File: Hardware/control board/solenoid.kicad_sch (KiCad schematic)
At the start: 7 parts, among them J11 Screw_Terminal_01x02, Q3 NMOS

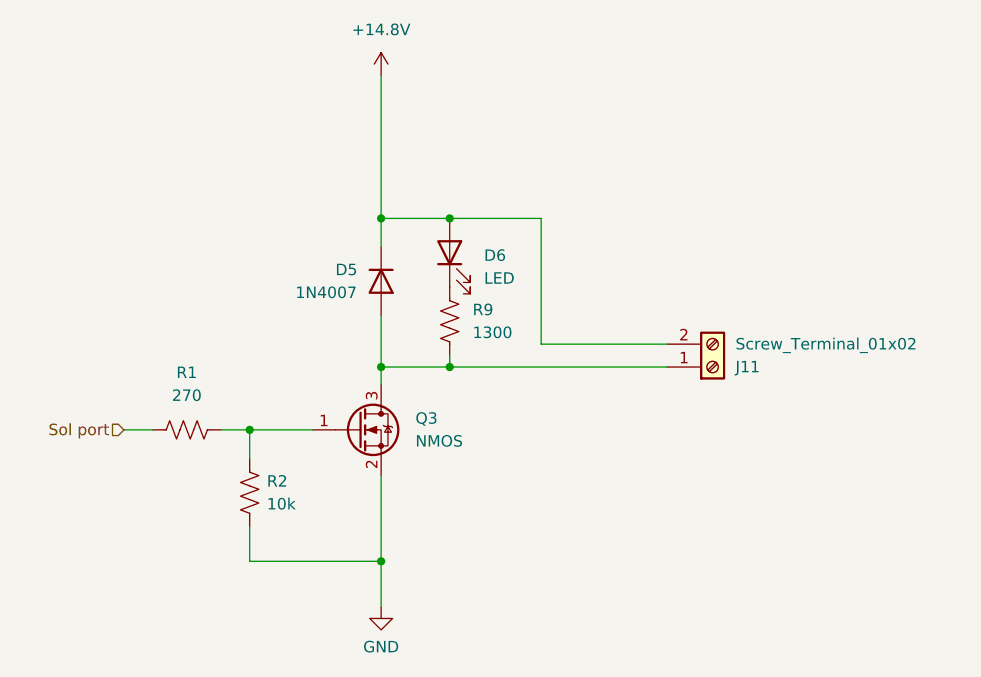
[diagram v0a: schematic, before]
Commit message: fixed github problems
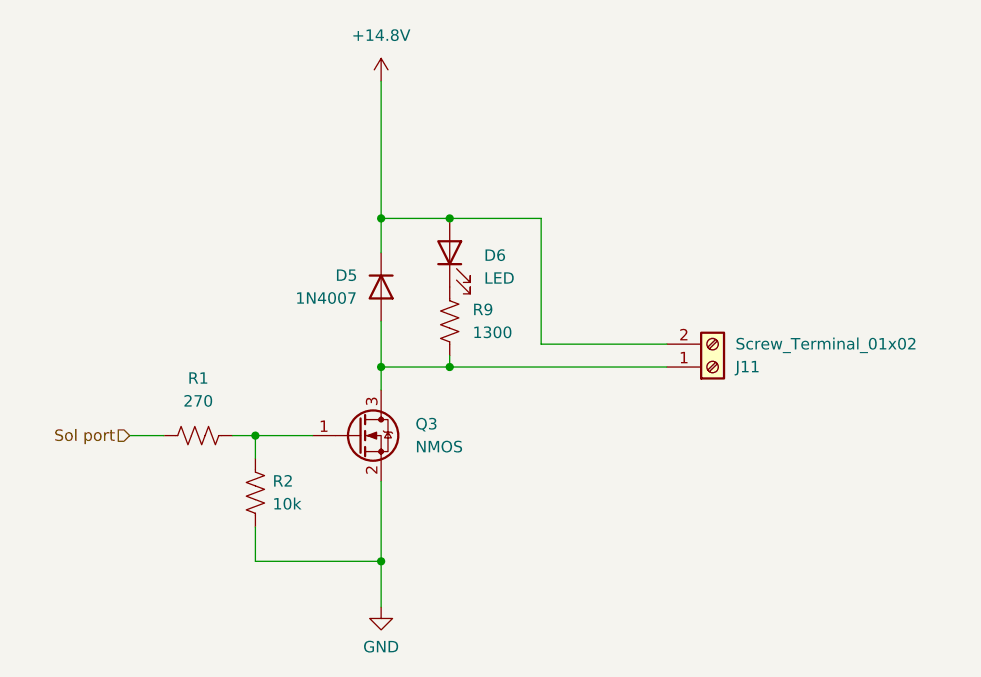
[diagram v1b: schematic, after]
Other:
- moved on the sheet: D5, Q3, R1, R2
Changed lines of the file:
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@@
   (junction (at 121.92 76.2) (diameter 0) (color 0 0 0 0)
   )
-  (junction (at 107.315 99.695) (diameter 0) (color 0 0 0 0)
-  )
   (junction (at 129.54 76.2) (diameter 0) (color 0 0 0 0)
   )
@@
   (junction (at 121.92 114.3) (diameter 0) (color 0 0 0 0)
   )
-  (wire (pts (xy 107.315 110.49) (xy 107.315 114.3))
-    (stroke (width 0) (type default))
-  )
-  (wire (pts (xy 107.315 99.695) (xy 114.3 99.695))
-    (stroke (width 0) (type default))
-  )
-  (wire (pts (xy 107.315 99.695) (xy 107.315 102.87))
-    (stroke (width 0) (type default))
-  )
-  (wire (pts (xy 107.315 114.3) (xy 121.92 114.3))
+  (junction (at 107.95 100.33) (diameter 0) (color 0 0 0 0)
+  )
+  (wire (pts (xy 107.95 110.49) (xy 107.95 114.3))
+    (stroke (width 0) (type default))
+  )
+  (wire (pts (xy 93.98 100.33) (xy 97.79 100.33))
+    (stroke (width 0) (type default))
+  )
+  (wire (pts (xy 107.95 114.3) (xy 121.92 114.3))
     (stroke (width 0) (type default))
   )
@@
     (stroke (width 0) (type default))
   )
-  (wire (pts (xy 93.345 99.695) (xy 96.52 99.695))
-    (stroke (width 0) (type default))
-  )
-  (wire (pts (xy 121.92 86.995) (xy 121.92 92.71))
-    (stroke (width 0) (type default))
-  )
-  (wire (pts (xy 121.92 92.71) (xy 121.92 94.615))
+  (wire (pts (xy 121.92 87.63) (xy 121.92 92.71))
+    (stroke (width 0) (type default))
+  )
+  (wire (pts (xy 121.92 92.71) (xy 121.92 95.25))
     (stroke (width 0) (type default))
   )
@@
     (stroke (width 0) (type default))
   )
+  (wire (pts (xy 121.92 60.96) (xy 121.92 76.2))
+    (stroke (width 0) (type default))
+  )
+  (wire (pts (xy 107.95 100.33) (xy 107.95 102.87))
+    (stroke (width 0) (type default))
+  )
   (wire (pts (xy 129.54 76.2) (xy 139.7 76.2))
     (stroke (width 0) (type default))
@@
     (stroke (width 0) (type default))
   )
-  (wire (pts (xy 107.315 99.695) (xy 104.14 99.695))
-    (stroke (width 0) (type default))
-  )
-  (wire (pts (xy 121.92 104.775) (xy 121.92 114.3))
+  (wire (pts (xy 105.41 100.33) (xy 107.95 100.33))
+    (stroke (width 0) (type default))
+  )
+  (wire (pts (xy 107.95 100.33) (xy 114.3 100.33))
+    (stroke (width 0) (type default))
+  )
+  (wire (pts (xy 121.92 105.41) (xy 121.92 114.3))
     (stroke (width 0) (type default))
   )
@@
     (stroke (width 0) (type default))
   )
-  (wire (pts (xy 121.92 76.2) (xy 121.92 79.375))
-    (stroke (width 0) (type default))
-  )
-  (wire (pts (xy 121.92 60.325) (xy 121.92 76.2))
-    (stroke (width 0) (type default))
-  )
-  (hierarchical_label "Sol port" (shape input) (at 93.345 99.695 180) (fields_autoplaced)
+  (wire (pts (xy 121.92 76.2) (xy 121.92 80.01))
+    (stroke (width 0) (type default))
+  )
+  (hierarchical_label "Sol port" (shape input) (at 93.98 100.33 180) (fields_autoplaced)
     (effects (font (size 1.27 1.27)) (justify right))
   )
-  (symbol (lib_id "Transistor_FET:2N7002") (at 119.38 99.695 0) (unit 1)
-    (in_bom yes) (on_board yes) (dnp no) (fields_autoplaced)
-    (property "Reference" "Q3" (at 125.73 98.425 0)
-      (effects (font (size 1.27 1.27)) (justify left))
-    )
-    (property "Value" "NMOS" (at 125.73 100.965 0)
-      (effects (font (size 1.27 1.27)) (justify left))
-    )
-    (property "Footprint" "Package_TO_SOT_SMD:SOT-23" (at 124.46 101.6 0)
+  (symbol (lib_id "Transistor_FET:2N7002") (at 119.38 100.33 0) (unit 1)
+    (in_bom yes) (on_board yes) (dnp no) (fields_autoplaced)
+    (property "Reference" "Q3" (at 125.73 99.06 0)
+      (effects (font (size 1.27 1.27)) (justify left))
+    )
+    (property "Value" "NMOS" (at 125.73 101.6 0)
+      (effects (font (size 1.27 1.27)) (justify left))
+    )
+    (property "Footprint" "Package_TO_SOT_SMD:SOT-23" (at 124.46 102.235 0)
       (effects (font (size 1.27 1.27) italic) (justify left) hide)
     )
-    (property "Datasheet" "https://www.onsemi.com/pub/Collateral/NDS7002A-D.PDF" (at 119.38 99.695 0)
+    (property "Datasheet" "https://www.onsemi.com/pub/Collateral/NDS7002A-D.PDF" (at 119.38 100.33 0)
       (effects (font (size 1.27 1.27)) (justify left) hide)
     )
-    (property "Sim.Device" "NMOS" (at 119.38 116.84 0)
-      (effects (font (size 1.27 1.27)) hide)
-    )
-    (property "Sim.Type" "VDMOS" (at 119.38 118.745 0)
-      (effects (font (size 1.27 1.27)) hide)
-    )
-    (property "Sim.Pins" "1=D 2=G 3=S" (at 119.38 114.935 0)
+    (property "Sim.Device" "NMOS" (at 119.38 117.475 0)
+      (effects (font (size 1.27 1.27)) hide)
+    )
+    (property "Sim.Type" "VDMOS" (at 119.38 119.38 0)
+      (effects (font (size 1.27 1.27)) hide)
+    )
+    (property "Sim.Pins" "1=D 2=G 3=S" (at 119.38 115.57 0)
       (effects (font (size 1.27 1.27)) hide)
     )
@@
     )
   )
-  (symbol (lib_id "Device:R_US") (at 100.33 99.695 90) (unit 1)
-    (in_bom yes) (on_board yes) (dnp no) (fields_autoplaced)
-    (property "Reference" "R1" (at 100.33 93.345 90)
+  (symbol (lib_id "Device:R_US") (at 101.6 100.33 90) (unit 1)
+    (in_bom yes) (on_board yes) (dnp no) (fields_autoplaced)
+    (property "Reference" "R1" (at 101.6 93.98 90)
       (effects (font (size 1.27 1.27)))
     )
-    (property "Value" "270" (at 100.33 95.885 90)
+    (property "Value" "270" (at 101.6 96.52 90)
       (effects (font (size 1.27 1.27)))
     )
-    (property "Footprint" "Resistor_SMD:R_0805_2012Metric" (at 100.584 98.679 90)
-      (effects (font (size 1.27 1.27)) hide)
-    )
-    (property "Datasheet" "~" (at 100.33 99.695 0)
+    (property "Footprint" "Resistor_SMD:R_0805_2012Metric" (at 101.854 99.314 90)
+      (effects (font (size 1.27 1.27)) hide)
+    )
+    (property "Datasheet" "~" (at 101.6 100.33 0)
       (effects (font (size 1.27 1.27)) hide)
     )
@@
     )
   )
-  (symbol (lib_id "Device:R_US") (at 107.315 106.68 0) (unit 1)
-    (in_bom yes) (on_board yes) (dnp no) (fields_autoplaced)
-    (property "Reference" "R2" (at 109.22 105.41 0)
-      (effects (font (size 1.27 1.27)) (justify left))
-    )
-    (property "Value" "10k" (at 109.22 107.95 0)
-      (effects (font (size 1.27 1.27)) (justify left))
-    )
-    (property "Footprint" "Resistor_SMD:R_0805_2012Metric" (at 108.331 106.934 90)
-      (effects (font (size 1.27 1.27)) hide)
-    )
-    (property "Datasheet" "~" (at 107.315 106.68 0)
+  (symbol (lib_id "Device:R_US") (at 107.95 106.68 0) (unit 1)
+    (in_bom yes) (on_board yes) (dnp no) (fields_autoplaced)
+    (property "Reference" "R2" (at 109.855 105.41 0)
+      (effects (font (size 1.27 1.27)) (justify left))
+    )
+    (property "Value" "10k" (at 109.855 107.95 0)
+      (effects (font (size 1.27 1.27)) (justify left))
+    )
+    (property "Footprint" "Resistor_SMD:R_0805_2012Metric" (at 108.966 106.934 90)
+      (effects (font (size 1.27 1.27)) hide)
+    )
+    (property "Datasheet" "~" (at 107.95 106.68 0)
       (effects (font (size 1.27 1.27)) hide)
     )
@@
     )
   )
-  (symbol (lib_id "power:+12V") (at 121.92 60.325 0) (unit 1)
-    (in_bom yes) (on_board yes) (dnp no) (fields_autoplaced)
-    (property "Reference" "#PWR09" (at 121.92 64.135 0)
-      (effects (font (size 1.27 1.27)) hide)
-    )
-    (property "Value" "+14.8V" (at 121.92 55.245 0)
+  (symbol (lib_id "power:+12V") (at 121.92 60.96 0) (unit 1)
+    (in_bom yes) (on_board yes) (dnp no) (fields_autoplaced)
+    (property "Reference" "#PWR09" (at 121.92 64.77 0)
+      (effects (font (size 1.27 1.27)) hide)
+    )
+    (property "Value" "+14.8V" (at 121.92 55.88 0)
       (effects (font (size 1.27 1.27)))
     )
-    (property "Footprint" "" (at 121.92 60.325 0)
-      (effects (font (size 1.27 1.27)) hide)
-    )
-    (property "Datasheet" "" (at 121.92 60.325 0)
+    (property "Footprint" "" (at 121.92 60.96 0)
+      (effects (font (size 1.27 1.27)) hide)
+    )
+    (property "Datasheet" "" (at 121.92 60.96 0)
       (effects (font (size 1.27 1.27)) hide)
     )
@@
     )
   )
-  (symbol (lib_id "Diode:1N4007") (at 121.92 83.185 270) (unit 1)
+  (symbol (lib_id "Diode:1N4007") (at 121.92 83.82 270) (unit 1)
     (in_bom yes) (on_board yes) (dnp no)
-    (property "Reference" "D5" (at 116.84 81.915 90)
-      (effects (font (size 1.27 1.27)) (justify left))
-    )
-    (property "Value" "1N4007" (at 112.395 84.455 90)
-      (effects (font (size 1.27 1.27)) (justify left))
-    )
-    (property "Footprint" "Diode_THT:D_DO-41_SOD81_P10.16mm_Horizontal" (at 117.475 83.185 0)
-      (effects (font (size 1.27 1.27)) hide)
-    )
-    (property "Datasheet" "http://www.vishay.com/docs/88503/1n4001.pdf" (at 121.92 83.185 0)
-      (effects (font (size 1.27 1.27)) hide)
-    )
-    (property "Sim.Device" "D" (at 121.92 83.185 0)
-      (effects (font (size 1.27 1.27)) hide)
-    )
-    (property "Sim.Pins" "1=K 2=A" (at 121.92 83.185 0)
-      (effects (font (size 1.27 1.27)) hide)
-    )
+    (property "Reference" "D5" (at 116.84 82.55 90)
+      (effects (font (size 1.27 1.27)) (justify left))
+    )
+    (property "Value" "1N4007" (at 112.395 85.09 90)
+      (effects (font (size 1.27 1.27)) (justify left))
+    )
+    (property "Footprint" "Diode_THT:D_DO-41_SOD81_P10.16mm_Horizontal" (at 117.475 83.82 0)
+      (effects (font (size 1.27 1.27)) hide)
+    )
+    (property "Datasheet" "http://www.vishay.com/docs/88503/1n4001.pdf" (at 121.92 83.82 0)
+      (effects (font (size 1.27 1.27)) hide)
+    )
+    (property "Sim.Device" "D" (at 121.92 83.82 0)
+      (effects (font (size 1.27 1.27)) hide)
+    )
+    (property "Sim.Pins" "1=K 2=A" (at 121.92 83.82 0)
+      (effects (font (size 1.27 1.27)) hide)
+    )
